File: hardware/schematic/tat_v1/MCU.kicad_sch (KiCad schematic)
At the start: 24 parts, among them J3 JST-SH 1x7P, SW2 SW_SPDT, SW3 SW_Push, U4 STM32U073CCUx, X1 32.768KHz

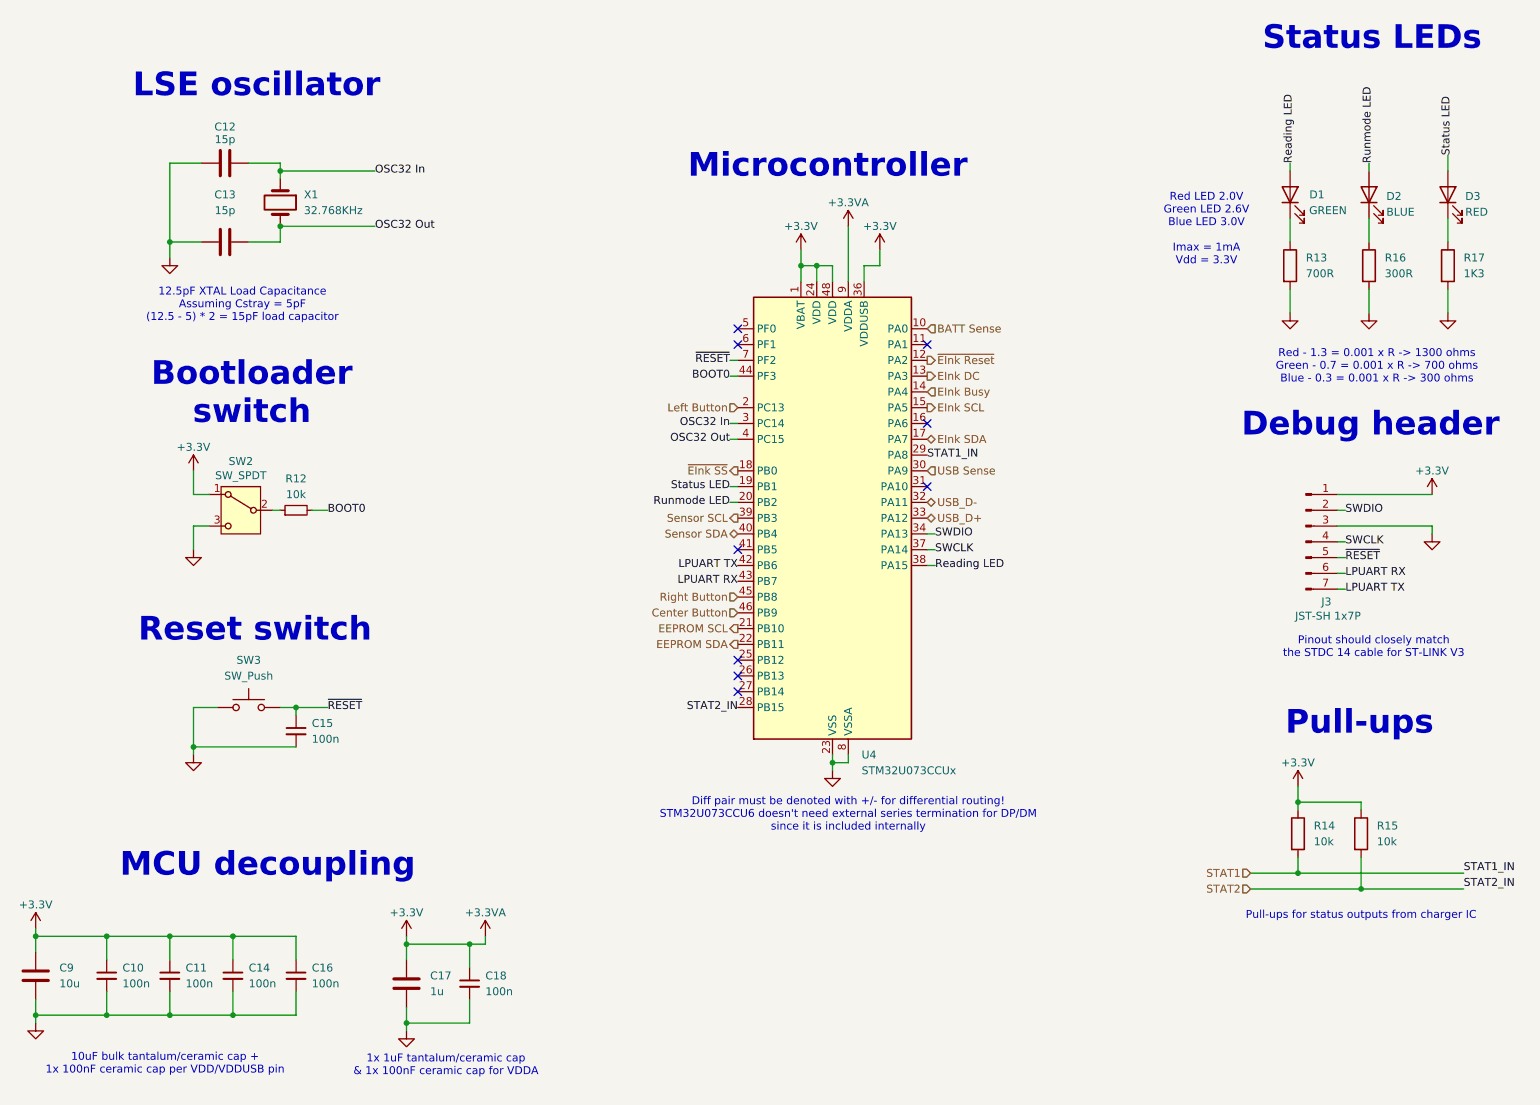
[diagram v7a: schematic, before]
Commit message: Fixed all ERC errors and warnings
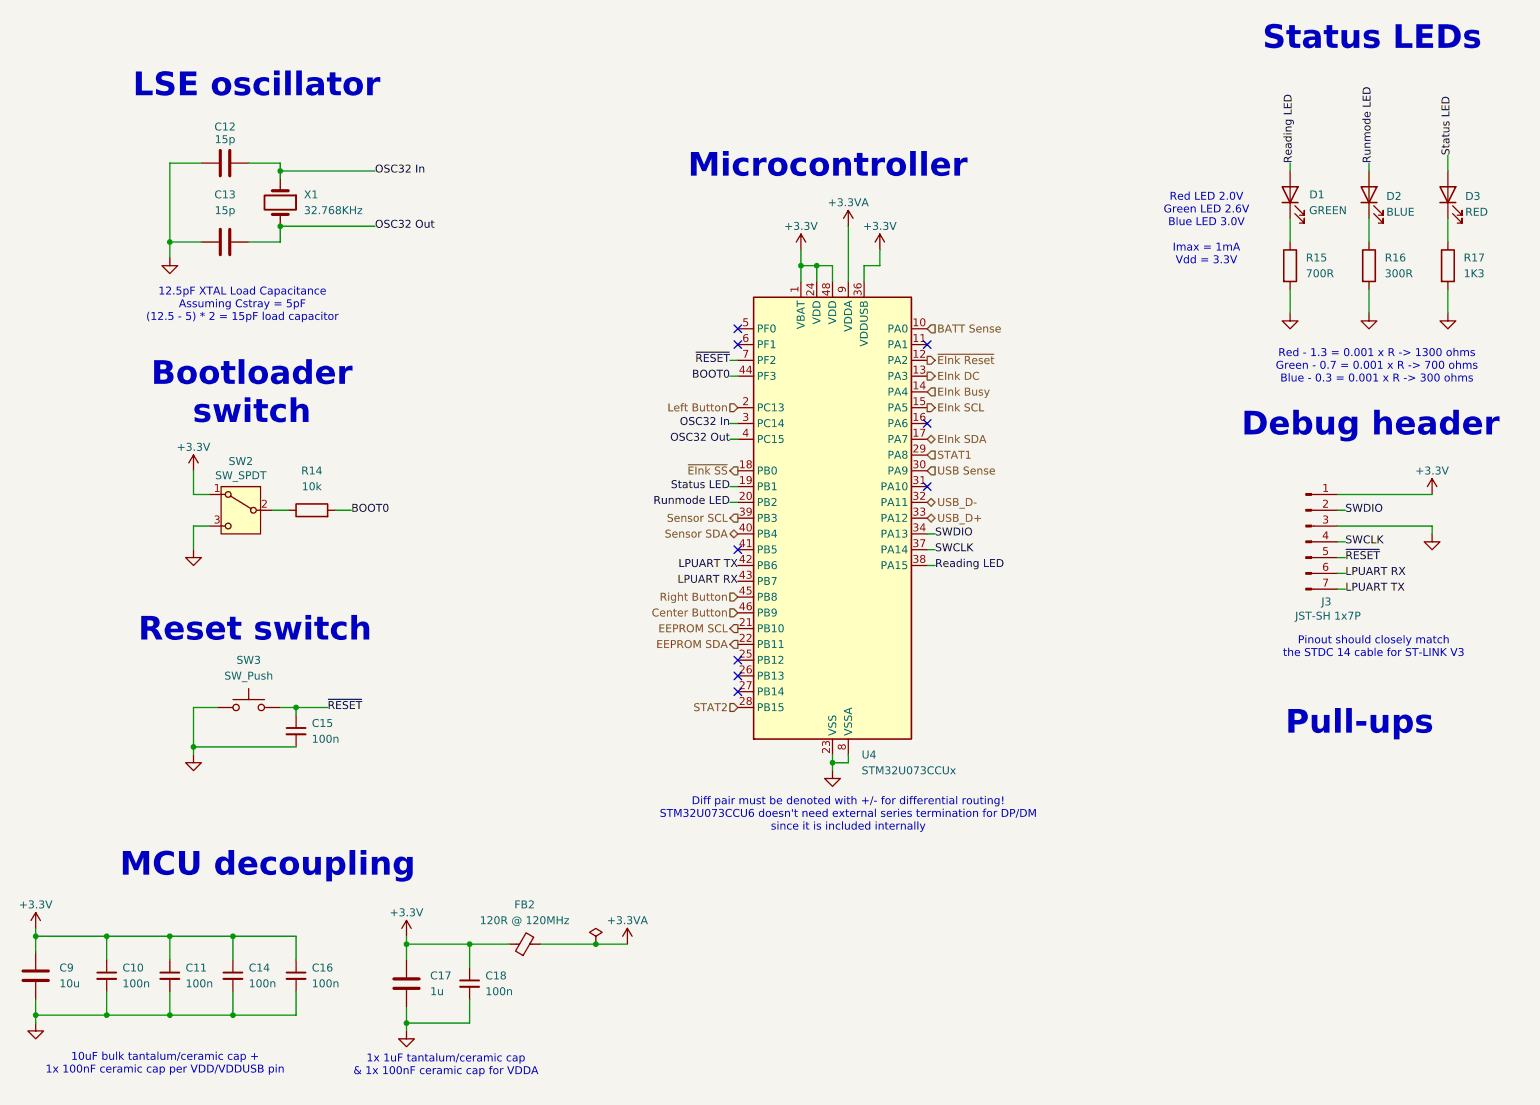
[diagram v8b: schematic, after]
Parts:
- removed R12: 10k, symbol Device:R_Small
- removed R15: 10k, symbol Device:R
- added FB2: 120R @ 120MHz, symbol Device:FerriteBead_Small
- renumbered R13 to R15
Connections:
- net +3.3V: now also FB2.1; no longer R14.1, U4.9 (VDDA)
- net BOOT0: now also R14.2
- net STAT1: no longer R14.2
- net at SW2.2 (B): now also R14.1
- new net +3.3VA: FB2.2, U4.9 (VDDA)
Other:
- note removed: "Pull-ups for status outputs from charger IC"
